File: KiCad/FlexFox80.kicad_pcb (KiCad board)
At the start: 4 copper layers, 111.2 x 80 mm, 168 parts, among them J101 DIN-5_180degree, J203 V4, J301 DB9_Female, J302 Conn_01x06, J303 DB9_Male, P203 Power Pole, P301 ISP/PDI, P302 Thru, P304 Header, Q101 LMN200B02, Q102 IRF610, Q201 MUN5213DW1, Q202 DMP4025LSD, Q203 RJK0354DSP, Q301 PN2222A, SW301 SPST, U107 LM5134B, U201 DAC081C085, U202 OPA171, U203 LTC3600, U204 MIC2196, U301 DS3231, U302 ATmega1284P-AU, U303 LP2992, U304 SI5351A, U305 74HC1G08, U306 LP2992, U307 SN74CB3Q3305, U308 LP2992, X301 ASTX-H11-25.MHZ, Y301 20 MHz

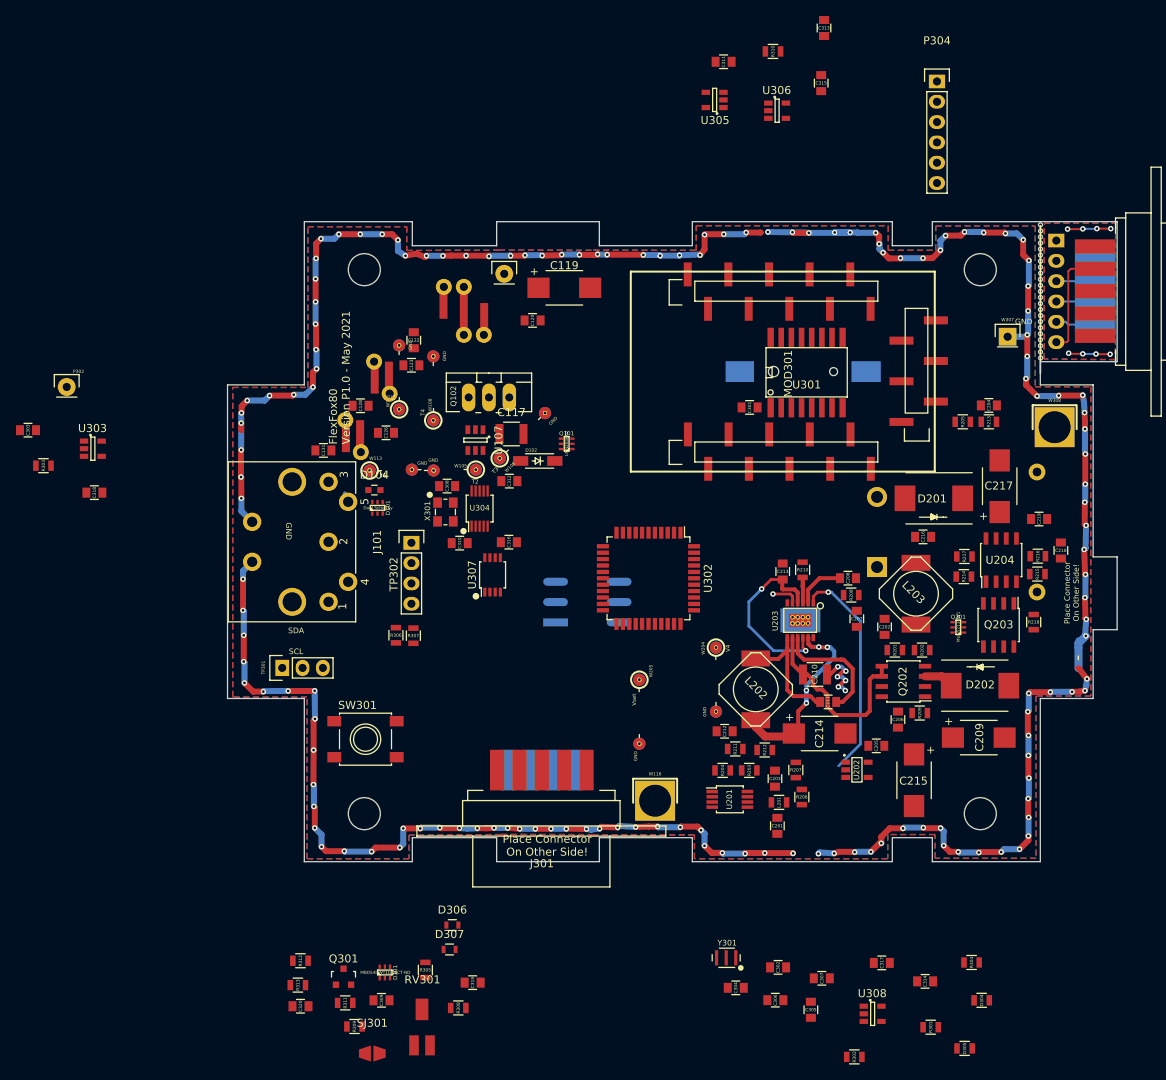
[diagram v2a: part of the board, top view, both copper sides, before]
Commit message: PCB Layout
Complete first pass at PCB parts layout. No traces.
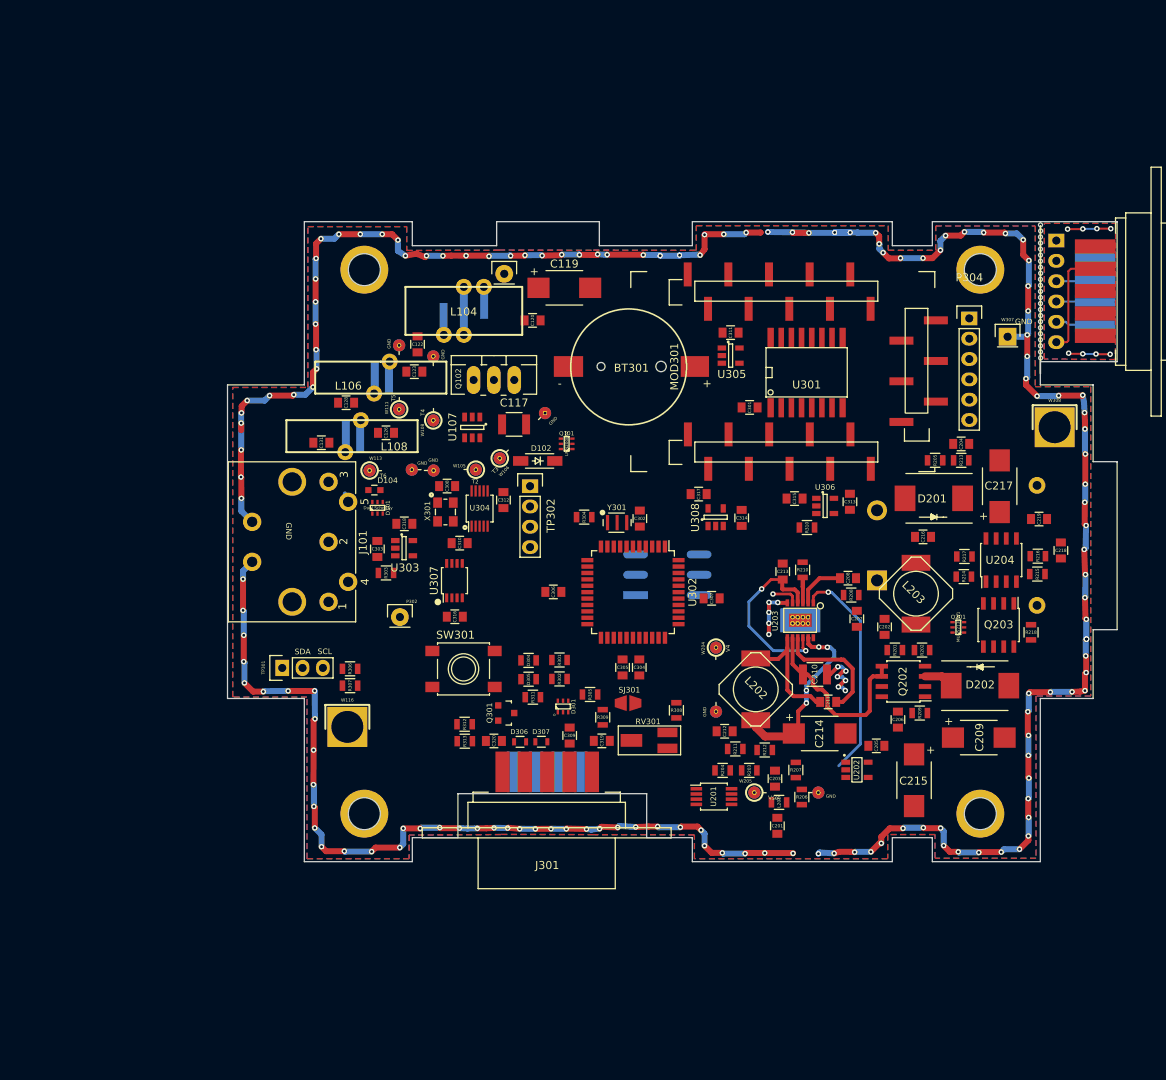
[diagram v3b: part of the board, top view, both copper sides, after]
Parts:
- BT301, L104, L106, L108: moved to F.Cu
- moved R304 73.8 mm to (60.8, 66.9)
- moved D305 71.4 mm to (53.8, 87.2)
- moved D304 70.8 mm to (53.8, 84.8)
- moved R301 65.3 mm to (57.7, 84.8)
- moved U308 65.1 mm to (77.2, 66.9), turned to 90 degrees
- moved C317 62.9 mm to (75.1, 64.0)
- moved C314 62.3 mm to (80.5, 67.0), turned to 270 degrees
- moved R302 59.9 mm to (57.7, 87.2)
- moved R310 59.7 mm to (88.6, 68.2)
- moved C313 59.3 mm to (94.0, 65.0), turned to 90 degrees
- moved C302 58.7 mm to (67.7, 67.1), turned to 270 degrees
- moved C306 58.1 mm to (56.9, 76.3)
- moved Y301 56.1 mm to (64.9, 67.6), turned to 180 degrees
- moved SJ301 54.2 mm to (66.3, 90.2)
- moved C315 52.0 mm to (87.1, 64.6), turned to 0 degrees
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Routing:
- net GND: track 394.5 -> 399.2 mm, vias 146 -> 153
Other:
- outline, holes or cut-outs redrawn
- board text removed: "Place Connector On Other Side!"
- board text removed: "Place Connector This Side"

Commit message: PCB Updates
Work in progress - routing
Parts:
- moved R206 6.65 mm to (94.6, 102.7)
- moved C216 4.92 mm to (108.1, 69.5)
- moved C201 3.80 mm to (81.2, 104.6)
- moved R207 3.51 mm to (89.8, 101.0)
- moved C120 3.09 mm to (52.0, 40.3), turned to 270 degrees
- moved W205 2.94 mm to (83.2, 98.7), turned to 270 degrees
- moved C205 2.60 mm to (97.3, 98.1)
- moved C203 2.46 mm to (82.7, 101.1), turned to 180 degrees
- moved L201 2.24 mm to (83.3, 103.9), turned to 90 degrees
- moved U202 1.72 mm to (93.3, 99.2)
- moved Q203 1.49 mm to (112.7, 81.9)
- moved R204 1.31 mm to (76.8, 98.7)
- moved R203 1.30 mm to (80.1, 98.7)
- moved D202 1.27 mm to (110.5, 89.2)
- moved C209 1.25 mm to (110.6, 95.6)
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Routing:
- net MAIN_PWR_ENABLE: track 0.00 -> 86.8 mm, vias 0 -> 3
- net TX_BATTERY_VOLTAGE: track 0.00 -> 50.5 mm, vias 0 -> 2
- net TX_+12_VOLTAGE: track 0.00 -> 46.3 mm, vias 0 -> 2
- net +12V: track 23.9 -> 63.7 mm, vias 0 -> 4
- net EXTERNAL_3.6V-15V_SUPPLY: track 0.00 -> 37.9 mm
- net TX_FINAL_VOLTAGE_ENABLE: track 3.40 -> 35.3 mm, vias 1 -> 2
- net Net-(C206-Pad1): track 0.00 -> 20.7 mm, vias 0 -> 2
- net Net-(Q202-Pad7): track 0.00 -> 20.4 mm, vias 0 -> 2
- net GND: track 399.2 -> 381.6 mm, vias 153 -> 141
- net Net-(R203-Pad1): track 0.00 -> 17.3 mm
- net Net-(D202-Pad2): track 0.00 -> 14.4 mm
- net +2to+12V: track 23.9 -> 36.0 mm
- net Net-(D201-Pad2): track 0.00 -> 11.4 mm
- net Net-(Q203-Pad4): track 0.00 -> 11.0 mm, vias 0 -> 2
- net Net-(C203-Pad2): track 0.00 -> 11.0 mm
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- added copper zone on B.Cu, net +12V
- added copper zone on F.Cu, net +12V
- added copper zone on B.Cu, net +2to+12V
- added copper zone on F.Cu, net +2to+12V
- added copper zone on F.Cu, net EXTERNAL_3.6V-15V_SUPPLY
- added copper zone on F.Cu, net Net-(C209-Pad1)
- added copper zone on F.Cu, net Net-(C211-Pad1)
- added copper zone on F.Cu, net Net-(D202-Pad2)

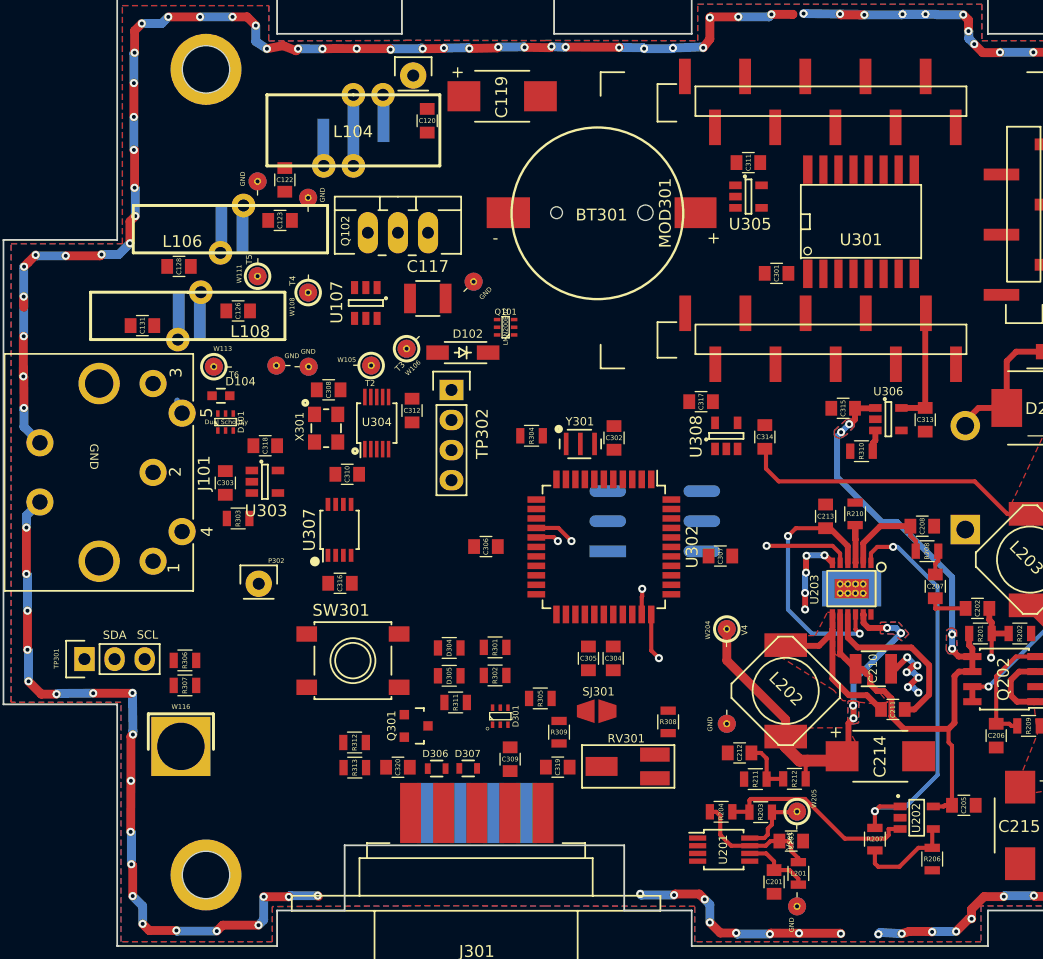
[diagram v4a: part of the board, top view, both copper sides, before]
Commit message: PCB Development
Added more traces
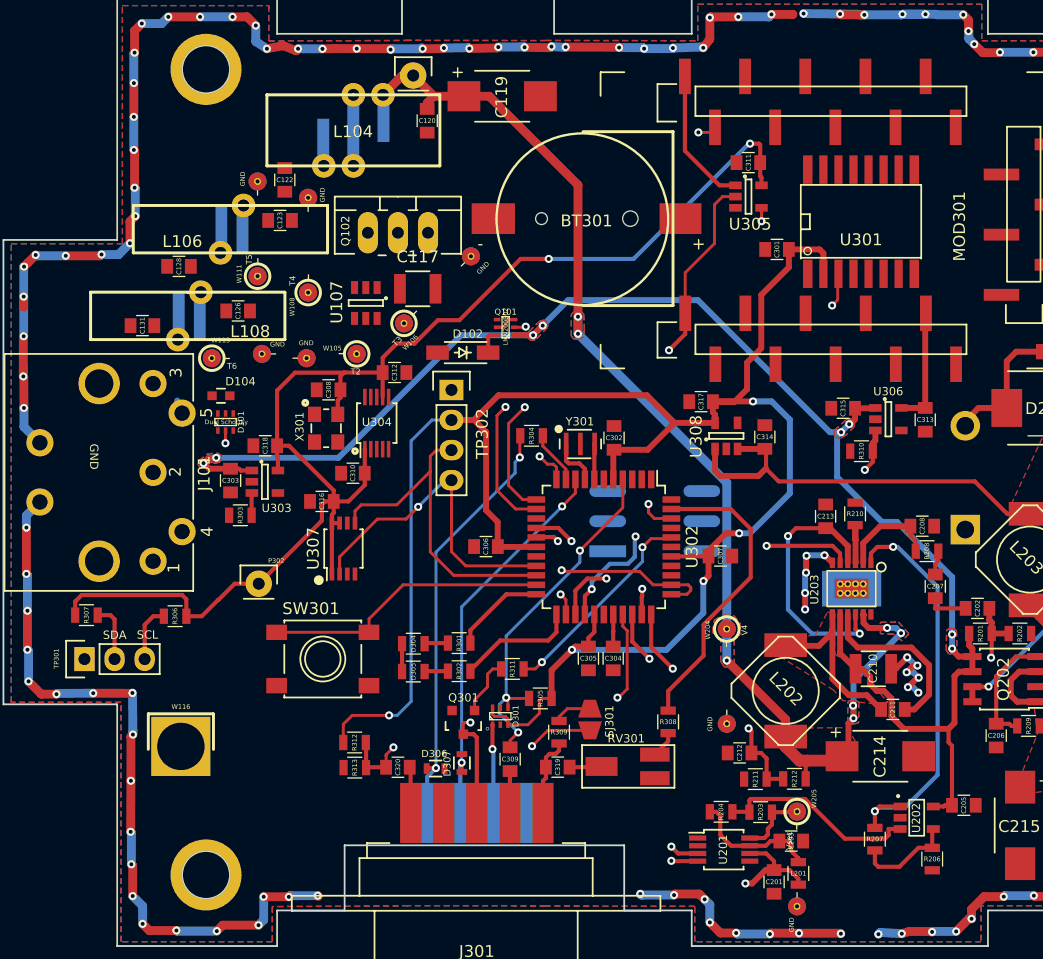
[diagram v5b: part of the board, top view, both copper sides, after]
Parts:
- moved R307 10.2 mm to (23.2, 82.1), turned to 0 degrees
- moved C316 7.08 mm to (43.1, 72.5), turned to 0 degrees
- moved R311 5.56 mm to (59.2, 86.6)
- moved Q301 3.99 mm to (55.0, 91.1), turned to 180 degrees
- moved R306 3.82 mm to (30.7, 82.2)
- moved C312 3.53 mm to (49.2, 61.6), turned to 0 degrees
- moved D304 3.05 mm to (50.8, 84.5)
- moved D305 3.05 mm to (50.8, 86.8)
- moved R301 3.05 mm to (54.7, 84.4)
- moved R302 3.05 mm to (54.7, 86.8)
- moved SW301 2.54 mm to (43.2, 85.8)
- moved W106 2.15 mm to (50.0, 57.4)
- moved C301 2.02 mm to (81.5, 51.2)
- moved U307 1.61 mm to (44.9, 76.5)
- moved W105 1.56 mm to (46.0, 60.0)
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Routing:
- net +3V3_L8: track 5.91 -> 186.9 mm, vias 0 -> 3
- net Vproc: track 0.00 -> 167.3 mm, vias 0 -> 5
- net +12V: track 63.7 -> 136.2 mm, vias 4 -> 8
- net DI_SDA: track 0.00 -> 66.4 mm, vias 0 -> 1
- net +2to+12V: track 36.0 -> 102.4 mm, vias 4 -> 7
- net DI_SCL: track 0.00 -> 62.6 mm, vias 0 -> 1
- net 80M_ANTENNA_DETECT: track 1.47 -> 52.5 mm, vias 0 -> 1
- net ~WIFI_RESET~: track 0.00 -> 42.1 mm, vias 0 -> 3
- net DI_TXD0: track 0.00 -> 40.9 mm, vias 0 -> 2
- net ~ANT_CONNECT_INT~: track 0.00 -> 37.0 mm, vias 0 -> 2
- net WIFI_ENABLE: track 1.84 -> 38.1 mm, vias 0 -> 2
- net TXD_TO_FTDI: track 0.00 -> 35.9 mm, vias 0 -> 2
- net PROC_HT_AUDIO_IN: track 0.00 -> 34.0 mm, vias 0 -> 2
- net RXD_TO_FTDI: track 0.00 -> 33.0 mm, vias 0 -> 2
- net /Digital/RXD1: track 0.00 -> 31.7 mm, vias 0 -> 2
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
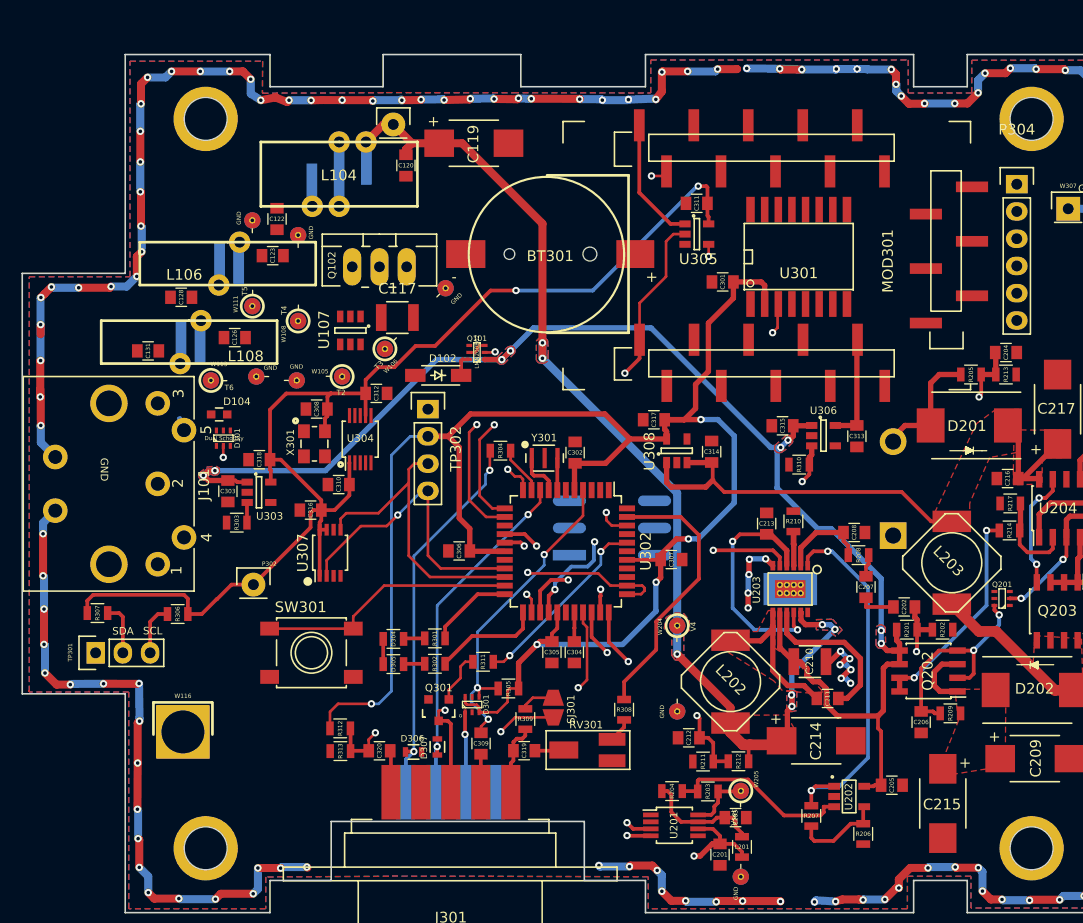
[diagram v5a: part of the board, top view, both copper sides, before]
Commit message: PCB Updates
First cut at routing complete. DRC passes. Need to add connection to pilot pin.
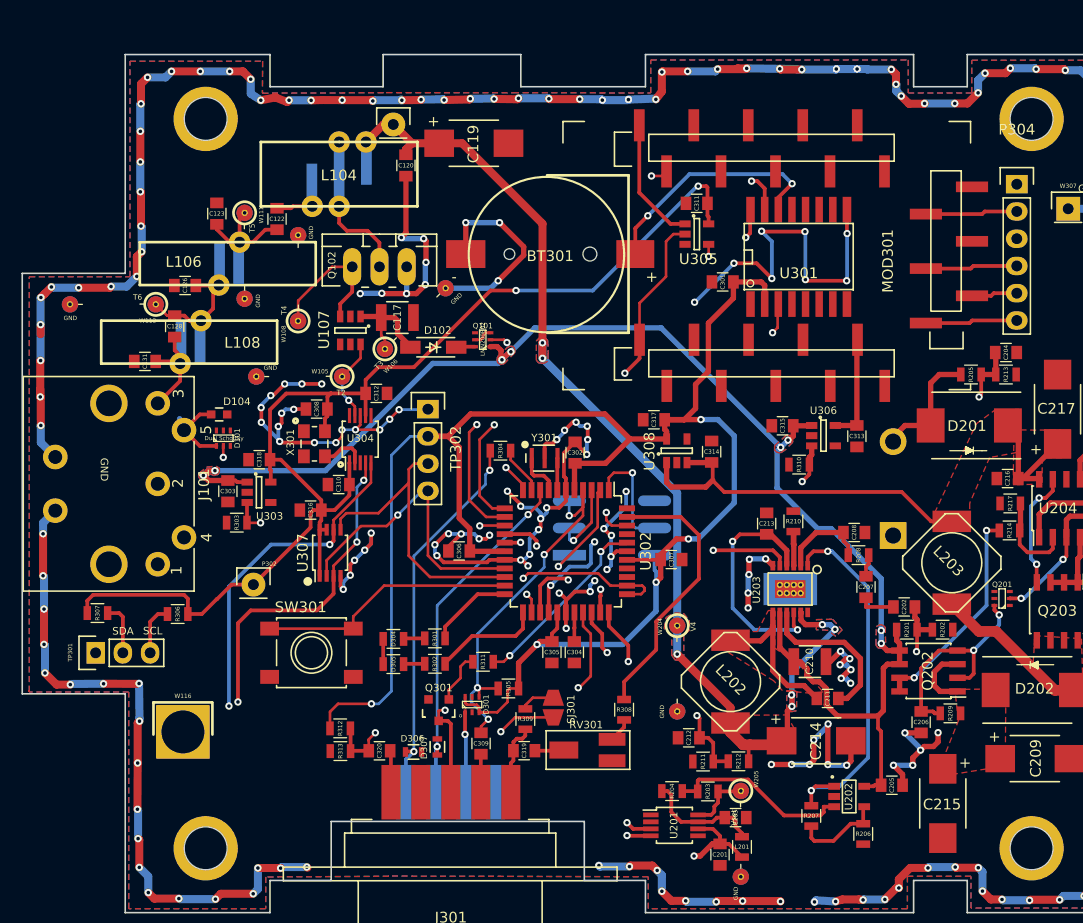
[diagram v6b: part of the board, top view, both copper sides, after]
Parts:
- moved W113 8.76 mm to (28.6, 53.3), turned to 180 degrees
- moved W111 8.73 mm to (36.9, 44.8), turned to 270 degrees
- moved C126 6.71 mm to (31.4, 51.5), turned to 0 degrees
- moved C123 6.52 mm to (34.3, 44.8), turned to 90 degrees
- moved C128 2.78 mm to (30.4, 55.3), turned to 90 degrees
- moved D102 2.66 mm to (54.5, 57.3)
- moved Q101 1.30 mm to (59.1, 56.6)
- moved C131 1.02 mm to (27.6, 58.6)
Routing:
- net GND: track 383.9 -> 596.0 mm, vias 141 -> 222
- net RTC_SDA: track 28.6 -> 74.4 mm, vias 0 -> 1
- net RTC_SCL: track 27.3 -> 69.5 mm, vias 1 -> 2
- net DI_SDA: track 66.4 -> 97.8 mm, vias 1 -> 3
- net DI_SCL: track 62.6 -> 93.5 mm, vias 1 -> 4
- net 3V3_PWR_ENABLE: track 1.89 -> 26.1 mm, vias 0 -> 2
- net Net-(BT301-Pad1): track 0.00 -> 22.4 mm, vias 0 -> 2
- net Net-(Q102-Pad1): track 0.00 -> 13.3 mm
- net Net-(C126-Pad2): track 0.00 -> 11.0 mm
- net MOSI: track 0.00 -> 10.6 mm, vias 0 -> 1
- net MISO: track 0.00 -> 10.2 mm, vias 0 -> 1
- net Net-(C122-Pad2): track 0.00 -> 9.98 mm
- net Net-(C117-Pad1): track 0.00 -> 9.65 mm
- net Net-(C128-Pad1): track 0.00 -> 9.62 mm
- net Net-(MOD301-Pad26): track 0.00 -> 8.58 mm
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
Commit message: PCB Updates
PCB is now ready for review. Still needs some silkscreen text added.
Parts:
- added J102: Conn_01x02, Pin_Headers:Pin_Header_Straight_1x02, F.Cu at (41.9, 56.3)
- moved W108 4.97 mm to (41.6, 49.9)
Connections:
- D301 pad 2: (no net) -> Net-(D301-Pad2)
- D301 pad 5: (no net) -> Net-(D301-Pad5)
- J101 pad 1: (no net) -> Net-(J101-Pad1)
- J101 pad 4: (no net) -> Net-(J101-Pad4)
- J301 pad 4: (no net) -> Net-(J301-Pad4)
- J303 pad 1: (no net) -> Net-(J303-Pad1)
- J303 pad 3: (no net) -> Net-(J303-Pad3)
- J303 pad 4: (no net) -> Net-(J303-Pad4)
- J303 pad 5: (no net) -> Net-(J303-Pad5)
- MOD301 pad 12: (no net) -> Net-(MOD301-Pad12)
- MOD301 pad 13: (no net) -> Net-(MOD301-Pad13)
- MOD301 pad 15: (no net) -> Net-(MOD301-Pad15)
- MOD301 pad 23: (no net) -> Net-(MOD301-Pad23)
- MOD301 pad 3: (no net) -> Net-(MOD301-Pad3)
- MOD301 pad 5: (no net) -> Net-(MOD301-Pad5)
- MOD301 pad 8: (no net) -> Net-(MOD301-Pad8)
- P304 pad 3: (no net) -> Net-(P304-Pad3)
- U107 pad 2: (no net) -> Net-(J102-Pad2)
- U201 pad 1: (no net) -> Net-(U201-Pad1)
- U201 pad 2: (no net) -> Net-(U201-Pad2)
- U203 pad 12: (no net) -> Net-(U203-Pad12)
- U302 pad 36: (no net) -> /Digital/PA1
- U302 pad 37: (no net) -> /Digital/PA0
- U302 pad 41: (no net) -> /Digital/PB1
- U302 pad 44: (no net) -> /Digital/PB4
- U303 pad 4: (no net) -> Net-(U303-Pad4)
- U304 pad 10: (no net) -> Net-(U304-Pad10)
- U304 pad 3: (no net) -> Net-(U304-Pad3)
- U304 pad 6: (no net) -> Net-(U304-Pad6)
- U306 pad 4: (no net) -> Net-(U306-Pad4)
- U308 pad 4: (no net) -> Net-(U308-Pad4)
- X301 pad 1: (no net) -> Net-(X301-Pad1)
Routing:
- net GND: track 596.0 -> 793.7 mm, vias 222 -> 314
- net Net-(J102-Pad2): track 0.00 -> 6.80 mm
- net Vproc: track 169.8 -> 163.1 mm
- net Net-(Q102-Pad1): track 13.3 -> 10.5 mm
- net 80M_ANTENNA_DETECT: track 59.7 -> 58.2 mm
- net PROC_TONE_OUT: track 25.6 -> 26.1 mm
